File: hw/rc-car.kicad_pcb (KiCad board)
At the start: 2 copper layers, 43.2 x 34.3 mm, 13 parts, among them P1 CONN_4X2, P2 CONN_2, P3 CONN_4, Q1 C8050, Q2 C8050, Q3 C8050, Q4 C8050, Q5 C8050

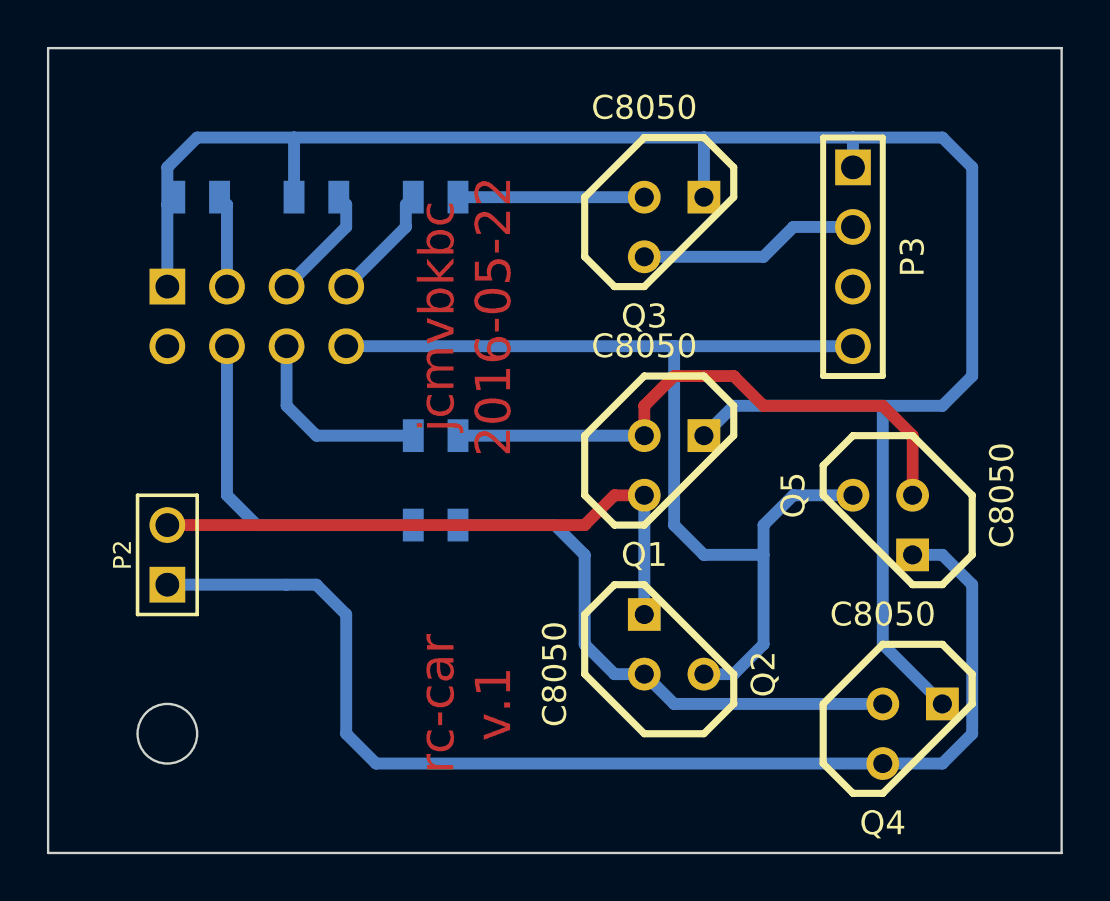
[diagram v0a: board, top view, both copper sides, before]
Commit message: fix bidirectional drive bug
Signed-off-by: Max Filippov <jcmvbkbc@gmail.com>
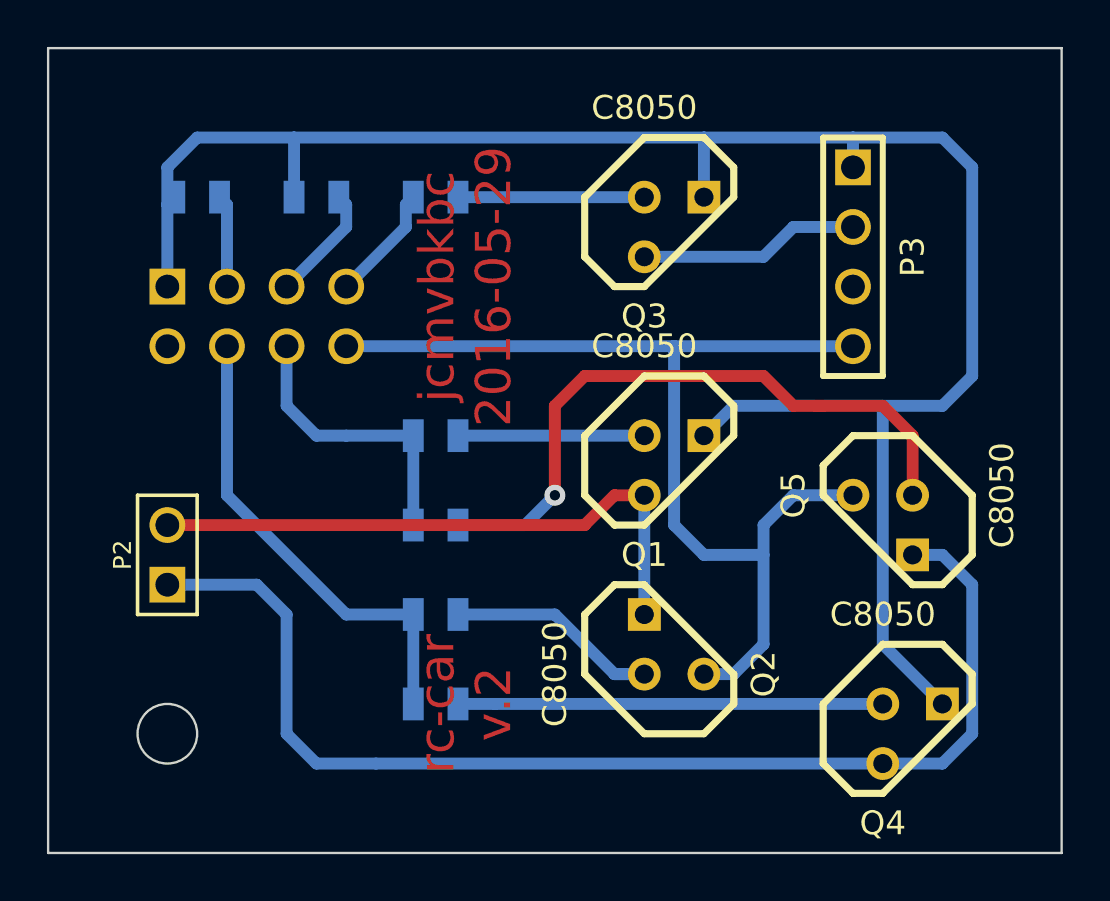
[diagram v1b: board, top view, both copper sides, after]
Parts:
- added R6: 250, SM0805, B.Cu at (66.0, 52.1)
- added R7: 250, SM0805, B.Cu at (66.0, 59.7)
- moved R5 7.62 mm to (66.0, 63.5), turned to 180 degrees
- moved R4 3.81 mm to (66.0, 55.9), turned to 180 degrees
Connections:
- P1 pad 4: N-000005 -> /BKWD
- P1 pad 6: N-000006 -> /FWD
- Q1 pad 2: /FWD -> N-000004
- Q2 pad 2: /BKWD -> N-000006
- Q4 pad 2: /BKWD -> N-0000017
- Q5 pad 2: /FWD -> N-0000016
- R4 pad 1: N-000006 -> N-0000016
- R5 pad 1: N-000005 -> N-0000017
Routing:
- net N-0000016: track 0.00 -> 28.1 mm, vias 0 -> 1
- net N-0000017: track 0.00 -> 18.1 mm
- net N-000005: track 14.8 -> 0.00 mm
- net /FWD: track 24.8 -> 12.3 mm
- net N-000004: track 0.00 -> 7.94 mm
- net /BKWD: track 23.5 -> 20.2 mm
- net N-000006: track 8.46 -> 10.3 mm
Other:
- board text added: "jcmvbkbc 2016-05-29"
- board text added: "rc-car v.2"
- board text removed: "jcmvbkbc 2016-05-22"
- board text removed: "rc-car v.1"

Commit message: hw: update schematic and plots
- use separate +5V for motors and +3.3V for ESP8266;
- add power terminals;
- use two-tact common collector drivers, drive them by common emitter
  voltage amplifiers.

Signed-off-by: Max Filippov <jcmvbkbc@gmail.com>
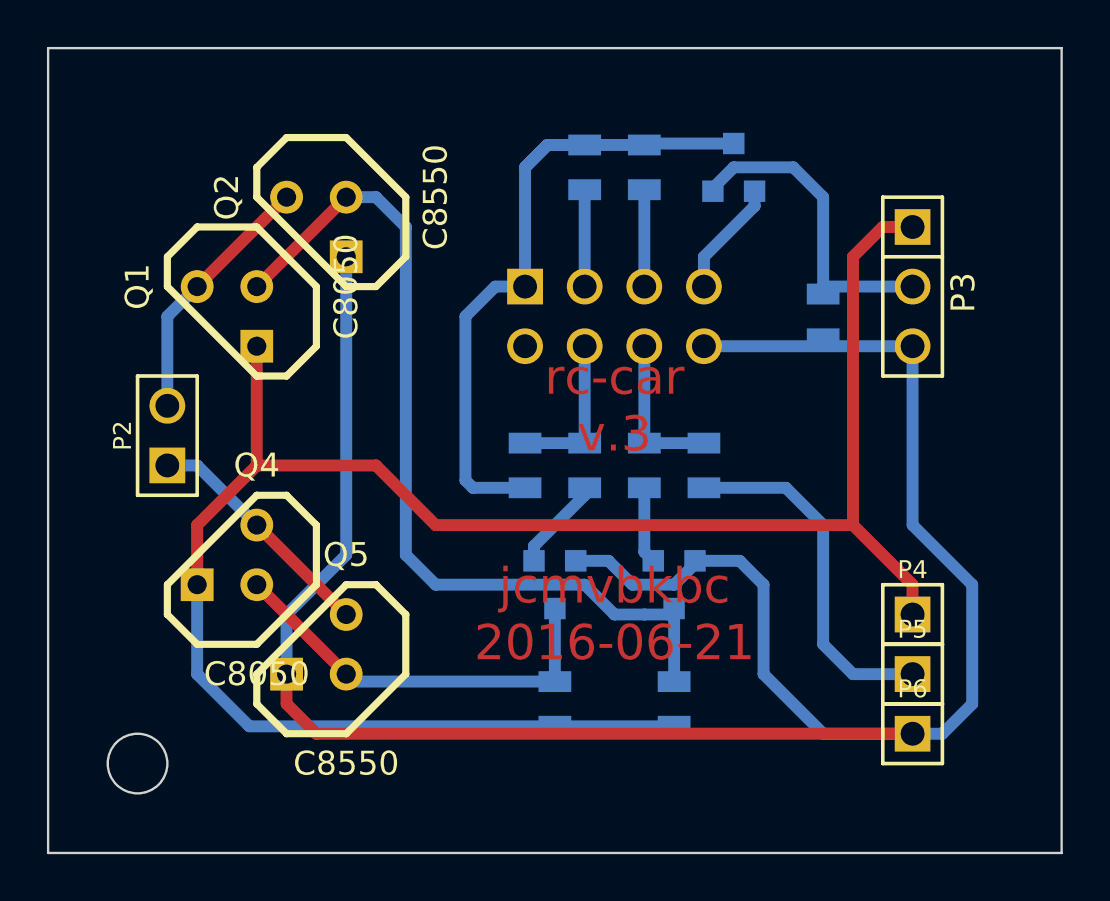
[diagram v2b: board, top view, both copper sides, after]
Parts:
- removed R3: 500, SM0805
- added P4: CONN_1, PIN_ARRAY_1, F.Cu at (86.4, 59.7)
- added P5: CONN_1, PIN_ARRAY_1, F.Cu at (86.4, 62.2)
- added P6: CONN_1, PIN_ARRAY_1, F.Cu at (86.4, 64.8)
- added Q6: MMBT2222, SOT23EBC, B.Cu at (71.1, 58.4)
- added Q7: MMBT2222, SOT23EBC, B.Cu at (78.7, 40.6)
- added R10: 1K, SM0805, B.Cu at (69.8, 53.3)
- added R8: 1K, SM0805, B.Cu at (71.1, 63.5)
- added R9: 1K, SM0805, B.Cu at (72.4, 53.3)
- P3: value CONN_4 -> CONN_3; footprint PIN_ARRAY_4x1 -> PIN_ARRAY_3X1
- Q2, Q5: value C8050 -> C8550
- Q3: value C8050 -> MMBT2222; footprint TO92-123 -> SOT23EBC; moved to B.Cu
- R4, R5, R6, R7: value 250 -> 1K
- moved Q4 30.2 mm to (57.1, 57.1), turned to 180 degrees
- moved Q5 24.7 mm to (61.0, 61.0), turned to 180 degrees
- moved Q2 23.4 mm to (61.0, 43.2), turned to 270 degrees
- moved R7 20.8 mm to (82.5, 47.0), turned to 270 degrees
- moved Q1 20.1 mm to (57.1, 47.0), turned to 270 degrees
- moved R2 16.6 mm to (72.4, 40.6), turned to 270 degrees
- moved R6 15.3 mm to (76.2, 63.5), turned to 90 degrees
- moved Q3 15.2 mm to (76.2, 58.4), turned to 180 degrees
- moved P1 15.2 mm to (73.7, 47.0)
- moved R1 14.0 mm to (74.9, 40.6), turned to 270 degrees
- moved R5 13.5 mm to (74.9, 53.3), turned to 90 degrees
- moved R4 11.7 mm to (77.5, 53.3), turned to 90 degrees
- moved P2 5.08 mm to (54.6, 52.1)
- moved P3 2.84 mm to (86.4, 45.7)
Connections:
- P1 pad 1: +5V -> +3.3V
- P1 pad 7: N-0000012 -> /STEER
- P3 pad 2: N-0000011 -> N-000008
- P3 pad 3: (no net) -> GND
- Q1 pad 2: N-000004 -> N-0000015
- Q2 pad 1: GND -> /MP
- Q2 pad 2: N-000006 -> N-0000015
- Q2 pad 3: /MP -> GND
- Q3 pad 1: N-0000011 -> GND
- Q3 pad 2: /STEER -> N-000006
- Q3 pad 3: +5V -> N-0000015
- Q4 pad 2: N-0000017 -> N-000009
- Q5 pad 1: GND -> /MN
- Q5 pad 2: N-0000016 -> N-000009
- Q5 pad 3: /MN -> GND
- R1 pad 1: +5V -> +3.3V
- R2 pad 1: +5V -> +3.3V
- R4 pad 1: N-0000016 -> +3.3V
- R5 pad 1: N-0000017 -> N-000006
- R5 pad 2: /BKWD -> /FWD
- R6 pad 1: /FWD -> +5V
- R6 pad 2: N-000004 -> N-0000015
- R7 pad 1: /BKWD -> N-000008
- R7 pad 2: N-000006 -> GND
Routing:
- net GND: track 49.1 -> 96.1 mm
- net +3.3V: track 0.00 -> 45.2 mm
- net /MN: track 50.4 -> 10.3 mm
- net N-0000015: track 0.00 -> 38.1 mm
- net N-0000016: track 28.1 -> 0.00 mm, vias 1 -> 0
- net N-0000017: track 18.1 -> 0.00 mm
- net N-000009: track 0.00 -> 17.5 mm
- net /MP: track 25.9 -> 11.0 mm
- net N-000008: track 0.00 -> 14.0 mm
- net /BKWD: track 20.2 -> 6.67 mm
- net N-0000011: track 9.42 -> 0.00 mm
- net N-000004: track 7.94 -> 0.00 mm
- net N-000006: track 10.3 -> 3.27 mm
- net /FWD: track 12.3 -> 6.67 mm
- net N-0000012: track 4.99 -> 0.00 mm
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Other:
- outline, holes or cut-outs redrawn
- board text added: "jcmvbkbc 2016-06-21"
- board text added: "rc-car v.3"
- board text removed: "jcmvbkbc 2016-05-29"
- board text removed: "rc-car v.2"
